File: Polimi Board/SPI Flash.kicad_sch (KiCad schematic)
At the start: 1 part, among them IC1 M95512-RMN6P

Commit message: Fatte modifiche
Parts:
- added C28: 100nF, symbol Device:C
- added R31, R32: R, symbol Device:R
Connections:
- net +3.3V: now also C28.1, R32.1; no longer IC1.8 (VCC)
- net GND: now also R31.2
- net at IC1.3 (~{W}): now also R31.1
- net at IC1.7 (~{HOLD}): now also R32.2
- new net: C28.2, IC1.8 (VCC)
- no-connect marks 2 -> 0
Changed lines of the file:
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@@
   (title_block
     (title "Polimi Board ")
-    (date "2024-04-24")
-    (rev "1.0")
+    (date "2024-04-29")
+    (rev "2.0")
     (company "Politecnico di Milano")
     (comment 1 "Embedded Systems Project")
     (comment 2 "ing. Zaccaria Eliseo Carrettoni")
   )
-  (no_connect (at 125.73 92.71))
-  (no_connect (at 153.67 90.17))
+  (wire (pts (xy 153.67 90.17) (xy 171.45 90.17))
+    (stroke (width 0) (type default))
+  )
   (wire (pts (xy 153.67 87.63) (xy 160.02 87.63))
     (stroke (width 0) (type default))
@@
     (stroke (width 0) (type default))
   )
+  (wire (pts (xy 171.45 90.17) (xy 171.45 86.36))
+    (stroke (width 0) (type default))
+  )
+  (wire (pts (xy 106.68 101.6) (xy 106.68 102.87))
+    (stroke (width 0) (type default))
+  )
+  (wire (pts (xy 106.68 93.98) (xy 106.68 92.71))
+    (stroke (width 0) (type default))
+  )
+  (wire (pts (xy 171.45 69.85) (xy 171.45 78.74))
+    (stroke (width 0) (type default))
+  )
   (wire (pts (xy 119.38 87.63) (xy 125.73 87.63))
     (stroke (width 0) (type default))
@@
     (stroke (width 0) (type default))
   )
-  (wire (pts (xy 160.02 83.82) (xy 160.02 87.63))
+  (wire (pts (xy 160.02 72.39) (xy 160.02 69.85))
+    (stroke (width 0) (type default))
+  )
+  (wire (pts (xy 106.68 92.71) (xy 125.73 92.71))
+    (stroke (width 0) (type default))
+  )
+  (wire (pts (xy 160.02 80.01) (xy 160.02 87.63))
     (stroke (width 0) (type default))
   )
   (wire (pts (xy 116.84 97.79) (xy 116.84 95.25))
     (stroke (width 0) (type default))
+  )
+  (text_box "In order to secure a stable DC supply voltage, it is\nrecommended to decouple the VCC line with a suitable capacitor (usually in the range between 10 and 100 nF)\nclose to the VCC / VSS device pins."
+    (at 116.84 63.5 0) (size 39.37 13.97)
+    (stroke (width 0) (type default))
+    (fill (type none))
+    (effects (font (size 1.27 1.27)) (justify left top))
   )
   (hierarchical_label "SDI" (shape input) (at 161.29 95.25 0) (fields_autoplaced)
@@
         (path "/319fe76e-1f98-44b3-99b0-af1a9ad7322c/6ede4352-cbae-4369-81ad-e8e15f2edc14"
           (reference "#PWR018") (unit 1)
-        )
-      )
-    )
-  )
-  (symbol (lib_id "power:+3.3V") (at 160.02 83.82 0) (unit 1)
-    (in_bom yes) (on_board yes) (dnp no) (fields_autoplaced)
-    (property "Reference" "#PWR053" (at 160.02 87.63 0)
-      (effects (font (size 1.27 1.27)) hide)
-    )
-    (property "Value" "+3.3V" (at 160.02 78.74 0)
-      (effects (font (size 1.27 1.27)))
-    )
-    (property "Footprint" "" (at 160.02 83.82 0)
-      (effects (font (size 1.27 1.27)) hide)
-    )
-    (property "Datasheet" "" (at 160.02 83.82 0)
-      (effects (font (size 1.27 1.27)) hide)
-    )
-    (pin "1")
-    (instances
-      (project "Polimi Board"
-        (path "/319fe76e-1f98-44b3-99b0-af1a9ad7322c/6ede4352-cbae-4369-81ad-e8e15f2edc14"
-          (reference "#PWR053") (unit 1)
         )
       )
@@
         )
       )
+    )
+  )
+  (symbol (lib_id "Device:C") (at 160.02 76.2 0) (unit 1)
+    (in_bom yes) (on_board yes) (dnp no) (fields_autoplaced)
+    (property "Reference" "C28" (at 163.83 74.93 0)
+      (effects (font (size 1.27 1.27)) (justify left))
+    )
+    (property "Value" "100nF" (at 163.83 77.47 0)
+      (effects (font (size 1.27 1.27)) (justify left))
+    )
+    (property "Footprint" "" (at 160.9852 80.01 0)
+      (effects (font (size 1.27 1.27)) hide)
+    )
+    (property "Datasheet" "~" (at 160.02 76.2 0)
+      (effects (font (size 1.27 1.27)) hide)
+    )
+    (pin "2")
+    (pin "1")
+    (instances
+      (project "Polimi Board"
+        (path "/319fe76e-1f98-44b3-99b0-af1a9ad7322c/6ede4352-cbae-4369-81ad-e8e15f2edc14"
+          (reference "C28") (unit 1)
+        )
+      )
+    )
+  )
+  (symbol (lib_id "Device:R") (at 106.68 97.79 0) (unit 1)
+    (in_bom yes) (on_board yes) (dnp no) (fields_autoplaced)
+    (property "Reference" "R31" (at 109.22 96.52 0)
+      (effects (font (size 1.27 1.27)) (justify left))
+    )
+    (property "Value" "R" (at 109.22 99.06 0)
+      (effects (font (size 1.27 1.27)) (justify left))
+    )
+    (property "Footprint" "" (at 104.902 97.79 90)
+      (effects (font (size 1.27 1.27)) hide)
+    )
+    (property "Datasheet" "~" (at 106.68 97.79 0)
+      (effects (font (size 1.27 1.27)) hide)
+    )
+    (pin "1")
+    (pin "2")
+    (instances
+      (project "Polimi Board"
+        (path "/319fe76e-1f98-44b3-99b0-af1a9ad7322c/6ede4352-cbae-4369-81ad-e8e15f2edc14"
+          (reference "R31") (unit 1)
+        )
+      )
+    )
+  )
+  (symbol (lib_id "power:+3.3V") (at 160.02 69.85 0) (unit 1)
+    (in_bom yes) (on_board yes) (dnp no) (fields_autoplaced)
+    (property "Reference" "#PWR025" (at 160.02 73.66 0)
+      (effects (font (size 1.27 1.27)) hide)
+    )
+    (property "Value" "+3.3V" (at 160.02 64.77 0)
+      (effects (font (size 1.27 1.27)))
+    )
+    (property "Footprint" "" (at 160.02 69.85 0)
+      (effects (font (size 1.27 1.27)) hide)
+    )
+    (property "Datasheet" "" (at 160.02 69.85 0)
+      (effects (font (size 1.27 1.27)) hide)
+    )
+    (pin "1")
+    (instances
+      (project "Polimi Board"
+        (path "/319fe76e-1f98-44b3-99b0-af1a9ad7322c/6ede4352-cbae-4369-81ad-e8e15f2edc14"
+          (reference "#PWR025") (unit 1)
+        )
+      )
+    )
+  )
+  (symbol (lib_id "power:GND") (at 106.68 102.87 0) (unit 1)
+    (in_bom yes) (on_board yes) (dnp no) (fields_autoplaced)
+    (property "Reference" "#PWR069" (at 106.68 109.22 0)
+      (effects (font (size 1.27 1.27)) hide)
+    )
+    (property "Value" "GND" (at 106.68 107.95 0)
+      (effects (font (size 1.27 1.27)))
+    )
+    (property "Footprint" "" (at 106.68 102.87 0)
+      (effects (font (size 1.27 1.27)) hide)
+    )
+    (property "Datasheet" "" (at 106.68 102.87 0)
+      (effects (font (size 1.27 1.27)) hide)
+    )
+    (pin "1")
+    (instances
+      (project "Polimi Board"
+        (path "/319fe76e-1f98-44b3-99b0-af1a9ad7322c/6ede4352-cbae-4369-81ad-e8e15f2edc14"
+          (reference "#PWR069") (unit 1)
+        )
+      )
+    )
+  )
+  (symbol (lib_id "Device:R") (at 171.45 82.55 0) (unit 1)
+    (in_bom yes) (on_board yes) (dnp no) (fields_autoplaced)
+    (property "Reference" "R32" (at 173.99 81.28 0)
+      (effects (font (size 1.27 1.27)) (justify left))
+    )
+    (property "Value" "R" (at 173.99 83.82 0)
+      (effects (font (size 1.27 1.27)) (justify left))
+    )
+    (property "Footprint" "" (at 169.672 82.55 90)
+      (effects (font (size 1.27 1.27)) hide)
+    )
+    (property "Datasheet" "~" (at 171.45 82.55 0)
+      (effects (font (size 1.27 1.27)) hide)
+    )
+    (pin "1")
+    (pin "2")
+    (instances
+      (project "Polimi Board"
+        (path "/319fe76e-1f98-44b3-99b0-af1a9ad7322c/6ede4352-cbae-4369-81ad-e8e15f2edc14"
+          (reference "R32") (unit 1)
+        )
+      )
+    )
+  )
+  (symbol (lib_id "power:+3.3V") (at 171.45 69.85 0) (unit 1)
+    (in_bom yes) (on_board yes) (dnp no) (fields_autoplaced)
+    (property "Reference" "#PWR090" (at 171.45 73.66 0)
+      (effects (font (size 1.27 1.27)) hide)
+    )
+    (property "Value" "+3.3V" (at 171.45 64.77 0)
+      (effects (font (size 1.27 1.27)))
+    )
+    (property "Footprint" "" (at 171.45 69.85 0)
+      (effects (font (size 1.27 1.27)) hide)
+    )
+    (property "Datasheet" "" (at 171.45 69.85 0)
+      (effects (font (size 1.27 1.27)) hide)
+    )
+    (pin "1")
+    (instances
+      (project "Polimi Board"
+        (path "/319fe76e-1f98-44b3-99b0-af1a9ad7322c/6ede4352-cbae-4369-81ad-e8e15f2edc14"
+          (reference "#PWR090") (unit 1)
+        )
+      )

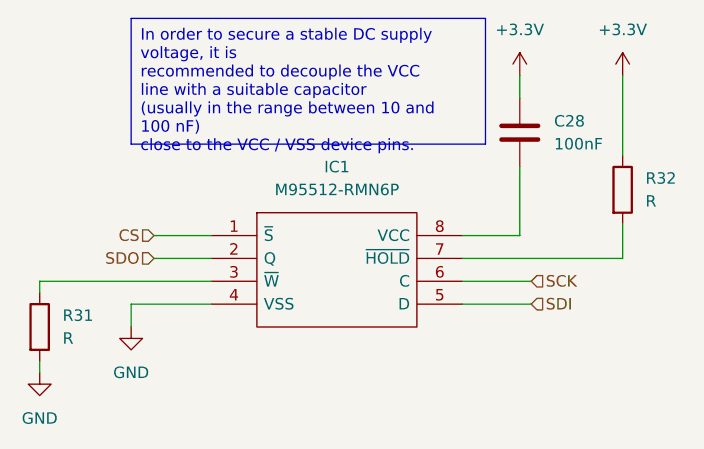
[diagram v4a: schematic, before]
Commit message: Added footprint from Mouser
readu for wiring
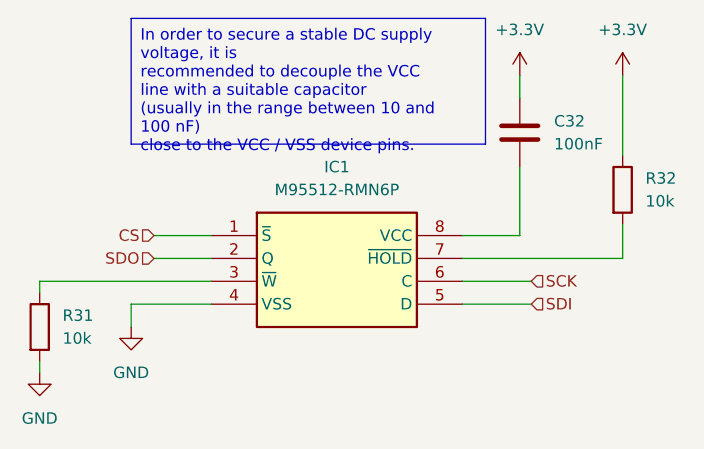
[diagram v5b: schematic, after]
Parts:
- removed IC1: M95512-RMN6P, SOIC127P600X175-8N, symbol Memory Polimi:M95512-RMN6P
- added IC1: M95512-RMN6P, SamacSys_Parts:SOIC127P600X175-8N, symbol SamacSys_Parts:M95512-RMN6P
- C32: renamed from C28; footprint (none) -> Capacitor_SMD:C_0603_1608Metric_Pad1.08x0.95mm_HandSolder
- R31, R32: value R -> 10k; footprint (none) -> Resistor_SMD:R_0603_1608Metric_Pad0.98x0.95mm_HandSolder
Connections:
- net CS: now also IC1.1 (~{S})
- net GND: now also IC1.4 (VSS)
- net SCK: now also IC1.6 (C)
- net SDI: now also IC1.5 (D)
- net SDO: now also IC1.2 (Q)
- net at R31.1: now also IC1.3 (~{W})
- net at R32.2: now also IC1.7 (~{HOLD})
- net at C32.2: now also IC1.8 (VCC)
